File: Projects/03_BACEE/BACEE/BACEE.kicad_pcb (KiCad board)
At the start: 2 copper layers, 42.4 x 26.4 mm, 17 parts, among them J1 Digital Pins, J2 Serial, J3 ICSP, J4 I2C, U1 DS1337_MLv1, U2 24LC1025, U3 24LC1025, U4 ATmega328P-AU, Y1 Crystal 32MHz, Y2 Crystal 16MHz

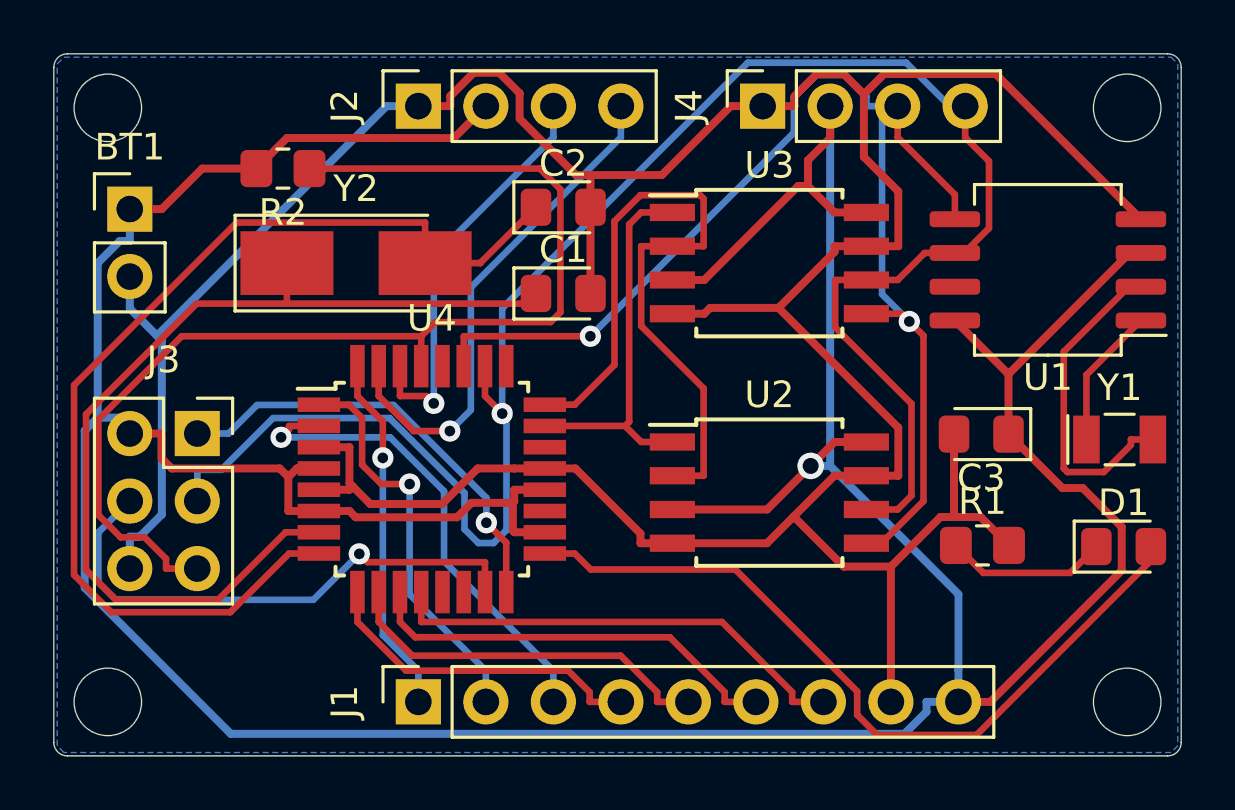
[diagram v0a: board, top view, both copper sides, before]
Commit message: Project 3: Add silkscreen text describing the PCB hardware
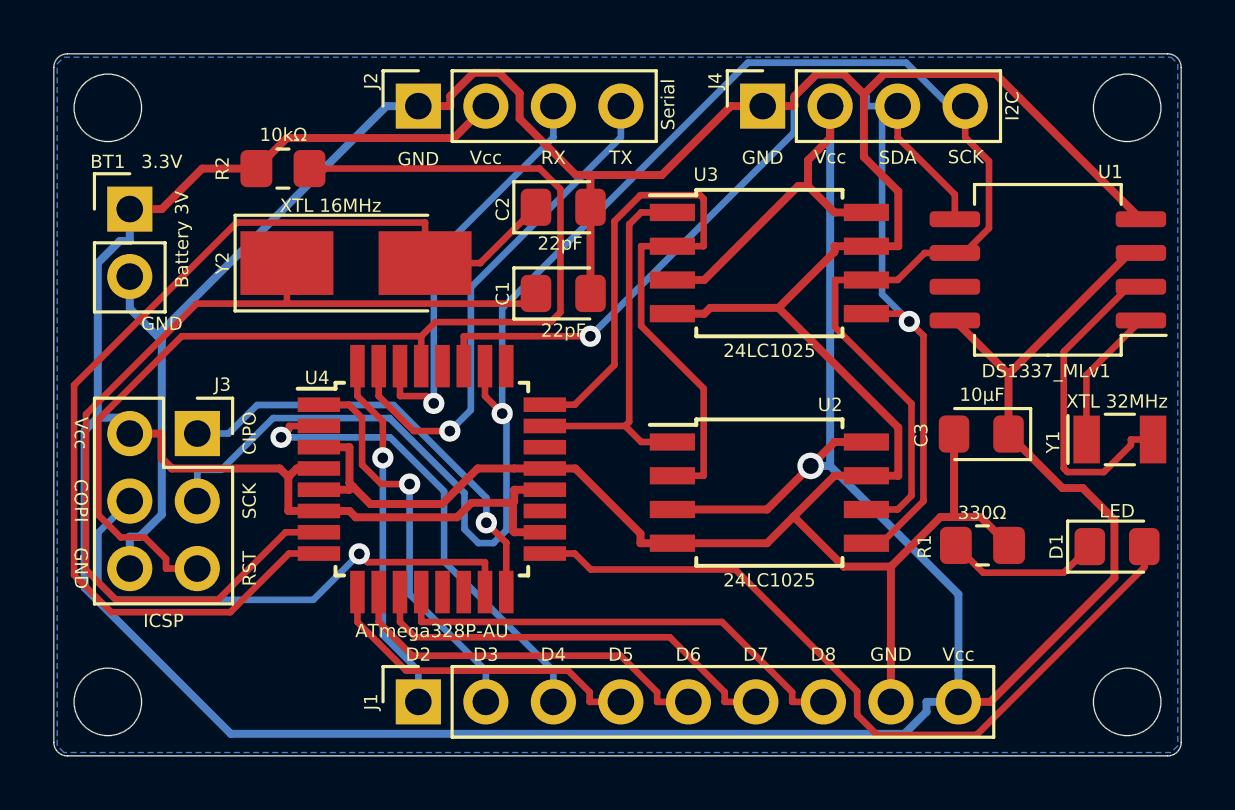
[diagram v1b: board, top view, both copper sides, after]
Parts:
- Y1: value Crystal 32MHz -> XTL 32MHz
- Y2: value Crystal 16MHz -> XTL 16MHz
- moved D1 0.25 mm to (242.7, 120.4)
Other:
- board text added: "10kΩ"
- board text added: "10μF"
- board text added: "22pF"
- board text added: "3.3V"
- board text added: "330Ω"
- board text added: "CIPO"
- board text added: "COPI"
- board text added: "D2"
- board text added: "D3"
- board text added: "D4"
- board text added: "D5"
- board text added: "D6"
- board text added: "D7"
- board text added: "D8"
- board text added: "GND"
- board text added: "RST"
- board text added: "RX"
- board text added: "SCK"
- board text added: "SDA"
- board text added: "TX"
- board text added: "Vcc"

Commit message: Project 3: Add graphics and board description on B.SilkS
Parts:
- added REF**: OSHW-Logo2_9.8x8mm_SilkScreen, Symbol:OSHW-Logo2_9.8x8mm_SilkScreen, B.Cu at (231.9, 121.4)
- added REF**: KiCad-Logo2_8mm_SilkScreen, Symbol:KiCad-Logo2_8mm_SilkScreen, B.Cu at (215.4, 115.1)
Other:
- board text added: "Arduino clone with: - 2Mbit EEPROM - Clock & Calendar - I2C, SPI, GPIO"
- board text added: "Designed by Michael Ly github.com/Michael-Q-Ly"
